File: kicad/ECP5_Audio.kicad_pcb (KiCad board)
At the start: 4 copper layers, 92 x 70 mm, 189 parts, among them J1 HDMI_A, J2 031-71052, J3 USB_B_RECEPTACLE, J4 USB_C_Receptacle, Q1 MMST2222A, SW1 Reset, T1 DA101JC, U1 TPS22948, U10 LP5907MFX-3.3, U11 FT2232HQ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

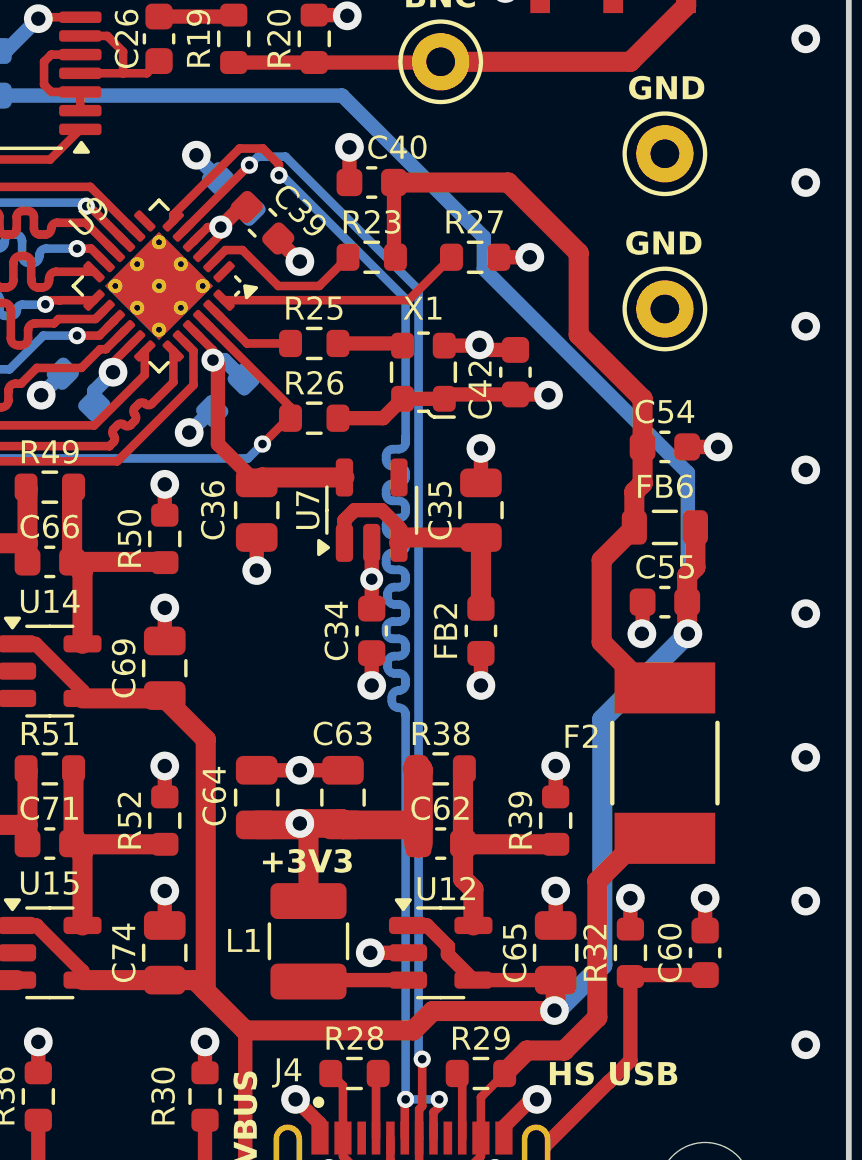
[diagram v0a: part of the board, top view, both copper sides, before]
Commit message: Moved 8.06K resistor close to USB3318C
Moved 8.06K resistor close to USB3318C
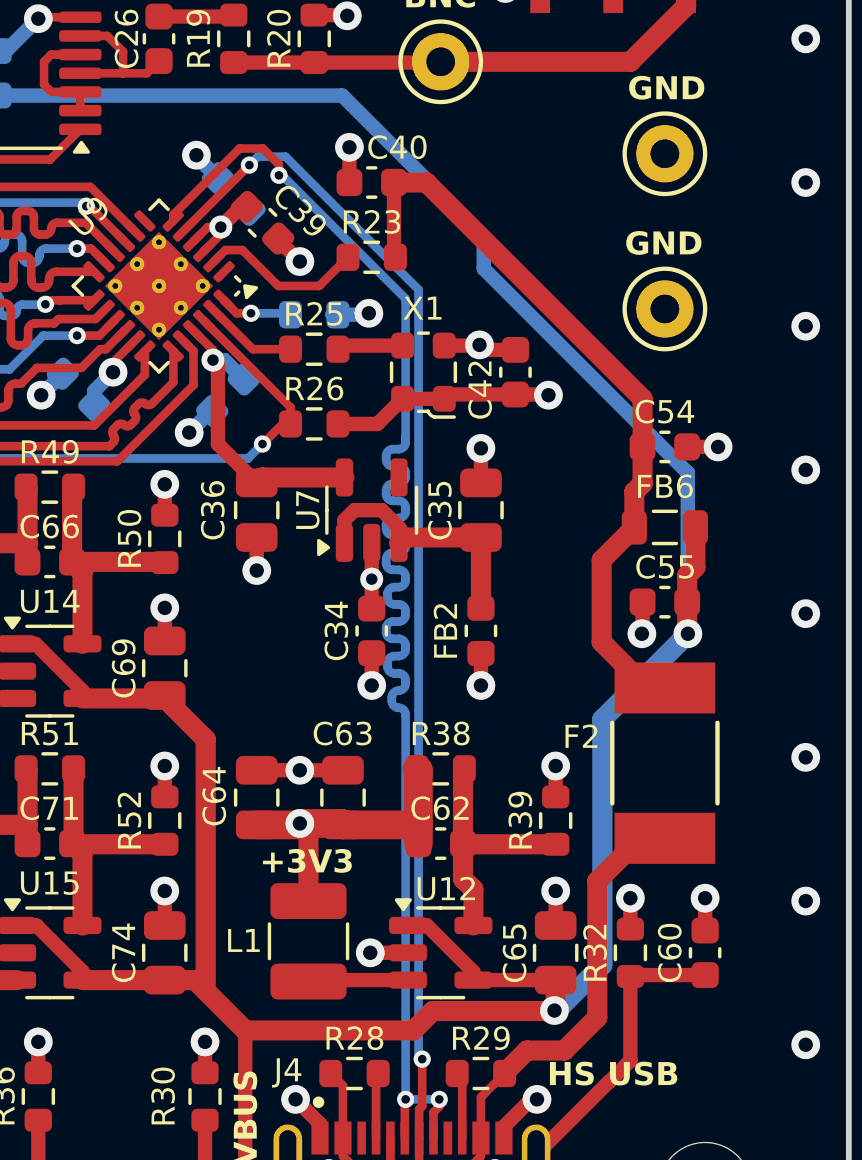
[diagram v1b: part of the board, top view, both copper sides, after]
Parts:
- R27: moved to B.Cu
- moved R27 5.95 mm to (123.4, 84.6)
- moved R25 0.20 mm to (123.4, 85.8)
- moved R26 0.20 mm to (123.4, 88.4)
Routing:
- net Net-(U9-RBIAS): track 8.53 -> 2.53 mm, vias 0 -> 1
- net ULPI_VBUS: track 28.3 -> 26.7 mm

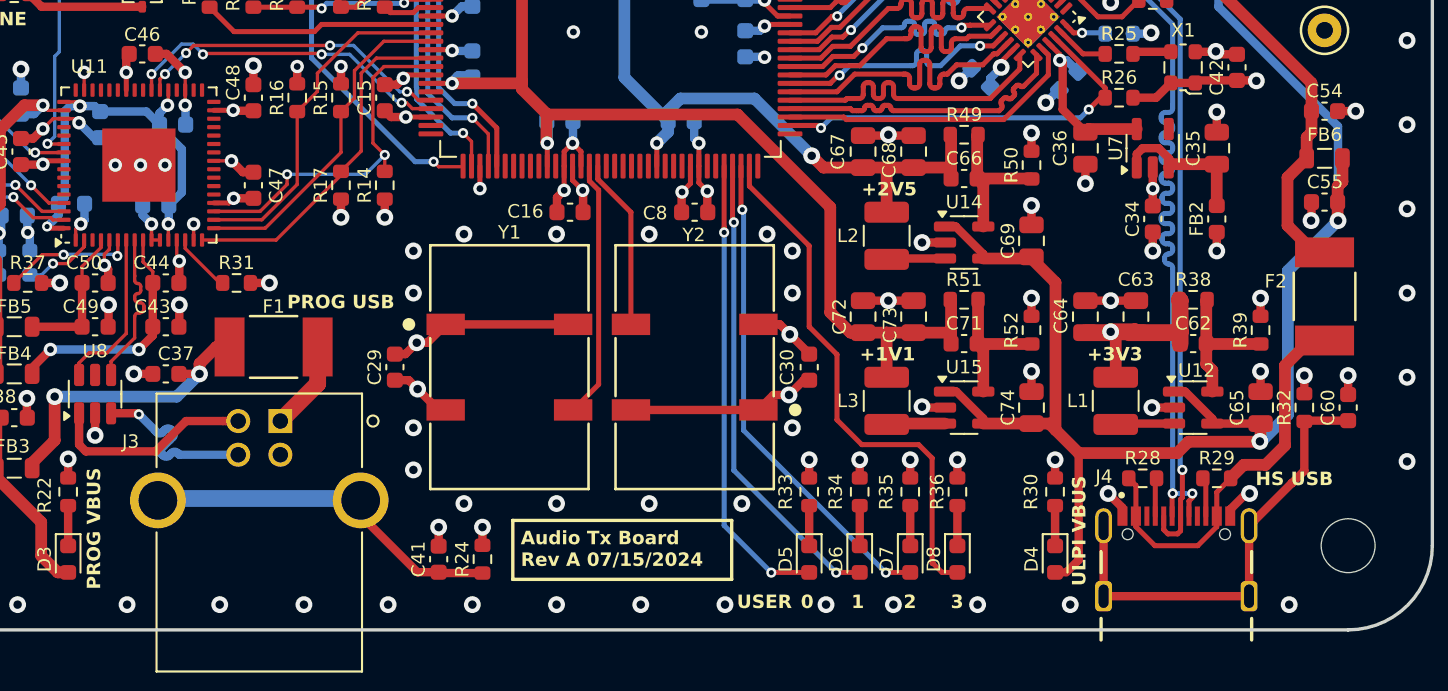
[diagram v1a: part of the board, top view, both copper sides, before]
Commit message: Prepared submission to PCBWay
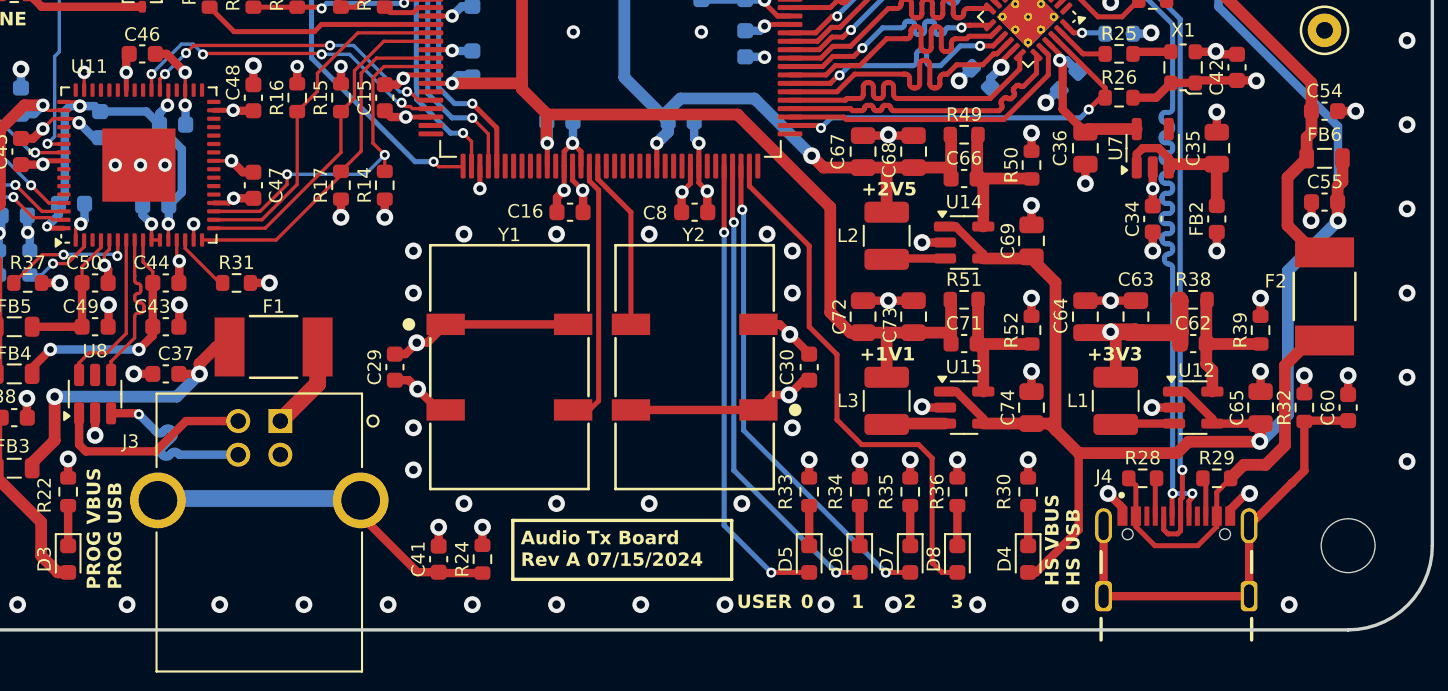
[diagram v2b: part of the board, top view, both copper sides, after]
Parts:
- moved D4 1.60 mm to (118.0, 115.8)
- moved R30 1.60 mm to (118.0, 111.8)
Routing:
- net +5V: track 153.3 -> 154.0 mm
- net 24.576MHz: track 15.3 -> 15.9 mm
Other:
- board text added: "HS VBUS"
- board text removed: "ULPI VBUS"
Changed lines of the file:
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@@
 	(footprint "Resistor_SMD:R_0603_1608Metric"
 		(layer "F.Cu")
-		(at 119.6 111.8 90)
+		(at 118 111.8 90)
 		(descr "Resistor SMD 0603 (1608 Metric), square (rectangular) end terminal, IPC_7351 nominal, (Body size source: IPC-SM-782 page 72, https://www.pcb-3d.com/wordpress/wp-content/uploads/ipc-sm-782a_amendment_1_and_2.pdf), generated with kicad-footprint-generator")
 		(tags "resistor")
@@
 		(tags "CCHD-950-50-100.000 ")
 		(property "Reference" "Y1"
-			(at 0 -8 0)
+			(at 0 -7.85 0)
 			(unlocked yes)
 			(layer "F.SilkS")
@@
 	(footprint "LED_SMD:LED_0603_1608Metric"
 		(layer "F.Cu")
-		(at 119.6 115.8 -90)
+		(at 118 115.8 -90)
 		(descr "LED SMD 0603 (1608 Metric), square (rectangular) end terminal, IPC_7351 nominal, (Body size source: http://www.tortai-tech.com/upload/download/2011102023233369053.pdf), generated with kicad-footprint-generator")
 		(tags "LED")
@@
 		)
 		(property "Value" "8.06K"
-			(at 0 -1.43 360)
+			(at 0 -1.43 0)
 			(layer "B.Fab")
 			(effects
@@
 		)
 		(fp_text user "${REFERENCE}"
-			(at 0 0 360)
+			(at 0 0 0)
 			(layer "B.Fab")
 			(effects
@@
 	)
 	(gr_text "PROG USB"
-		(at 74 101 0)
+		(at 64.25 117.6 90)
 		(layer "F.SilkS" knockout)
 		(effects
@@
 	)
 	(gr_text "HS USB"
-		(at 131.5 111.5 0)
+		(at 121.15 117.4 90)
 		(layer "F.SilkS" knockout)
 		(effects
@@
 		)
 	)
-	(gr_text "ULPI VBUS"
-		(at 121.5 117.4 90)
+	(gr_text "HS VBUS"
+		(at 119.9 117.4 90)
 		(layer "F.SilkS" knockout)
 		(effects
@@
 	)
 	(segment
-		(start 119.6 110.975)
-		(end 119.6 109.9)
+		(start 118 110.975)
+		(end 118 109.9)
 		(width 0.5)
 		(layer "F.Cu")
@@
 	)
 	(via
-		(at 119.6 109.9)
+		(at 118 109.9)
 		(size 1)
 		(drill 0.5)
@@
 	)
 	(segment
-		(start 119.6 116.5875)
-		(end 120.0625 116.5875)
+		(start 118 116.5875)
+		(end 118.4625 116.5875)
 		(width 0.5)
 		(layer "F.Cu")
@@
 	)
 	(segment
+		(start 118.4625 116.5875)
+		(end 121 114.05)
+		(width 0.5)
+		(layer "F.Cu")
+		(net 5)
+	)
+	(segment
 		(start 115.3375 107.75)
 		(end 115.3375 107.450001)
@@
 	)
 	(segment
-		(start 121 115.85)
-		(end 121 109.5)
-		(width 0.5)
-		(layer "F.Cu")
-		(net 5)
-	)
-	(segment
 		(start 136.375 95.675)
 		(end 136.4 95.7)
@@
 	)
 	(segment
+		(start 121 114.05)
+		(end 121 109.5)
+		(width 0.5)
+		(layer "F.Cu")
+		(net 5)
+	)
+	(segment
 		(start 136.375 93.675)
 		(end 136.375 94.6)
@@
 	)
 	(segment
-		(start 120.2625 116.5875)
-		(end 121 115.85)
-		(width 0.5)
-		(layer "F.Cu")
-		(net 5)
-	)
-	(segment
 		(start 126.85 109.5)
 		(end 121 109.5)
@@
 	)
 	(segment
-		(start 119.6 115.0125)
-		(end 119.6 112.625)
+		(start 118 115.0125)
+		(end 118 112.625)
 		(width 0.5)
 		(layer "F.Cu")
@@
 	)
 	(segment
-		(start 69.054 85.773)
-		(end 69 85.827)
+		(start 81.023 88.923)
+		(end 81.309712 88.923)
 		(width 0.2)
 		(layer "F.Cu")
@@
 	)
 	(segment
-		(start 81.086712 88.7)
-		(end 81.436712 89.05)
+		(start 69.054 85.773)
+		(end 69 85.827)
 		(width 0.2)
 		(layer "F.Cu")
@@
 	)
 	(segment
+		(start 81.309712 88.923)
+		(end 81.436712 89.05)
+		(width 0.2)
+		(layer "F.Cu")
+		(net 82)
+	)
+	(segment
 		(start 81.436712 89.05)
 		(end 82.5375 89.05)
@@
 	(segment
 		(start 80.8 88.7)
-		(end 81.086712 88.7)
+		(end 81.023 88.923)
 		(width 0.2)
 		(layer "F.Cu")
@@
 	)
 	(segment
+		(start 92.5 93.892577)
+		(end 92.5 106.4)
+		(width 0.3)
+		(layer "F.Cu")
+		(net 86)
+	)
+	(segment
 		(start 91.95 92.4625)
 		(end 91.95 93.342577)
@@
 	)
 	(segment
-		(start 92.5 93.892577)
-		(end 92.5 105.4246)
+		(start 91.96 106.94)
+		(end 90.9846 106.94)
 		(width 0.3)
 		(layer "F.Cu")
@@
 	)
 	(segment
-		(start 92.5 105.4246)
-		(end 90.9846 106.94)
+		(start 92.5 106.4)
+		(end 91.96 106.94)
 		(width 0.3)
 		(layer "F.Cu")

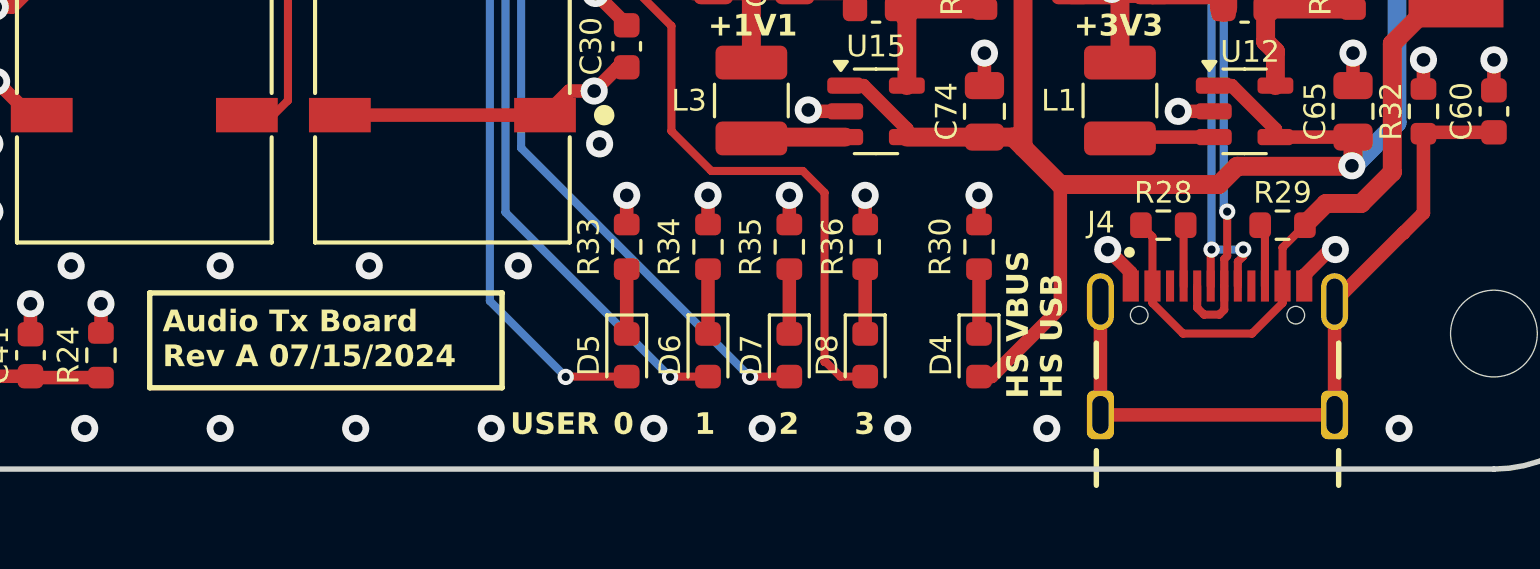
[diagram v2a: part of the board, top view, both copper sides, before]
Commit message: 5.1K USB resistors
Replaces 22K resistors to VBUS with 5.1K resistors to GND.
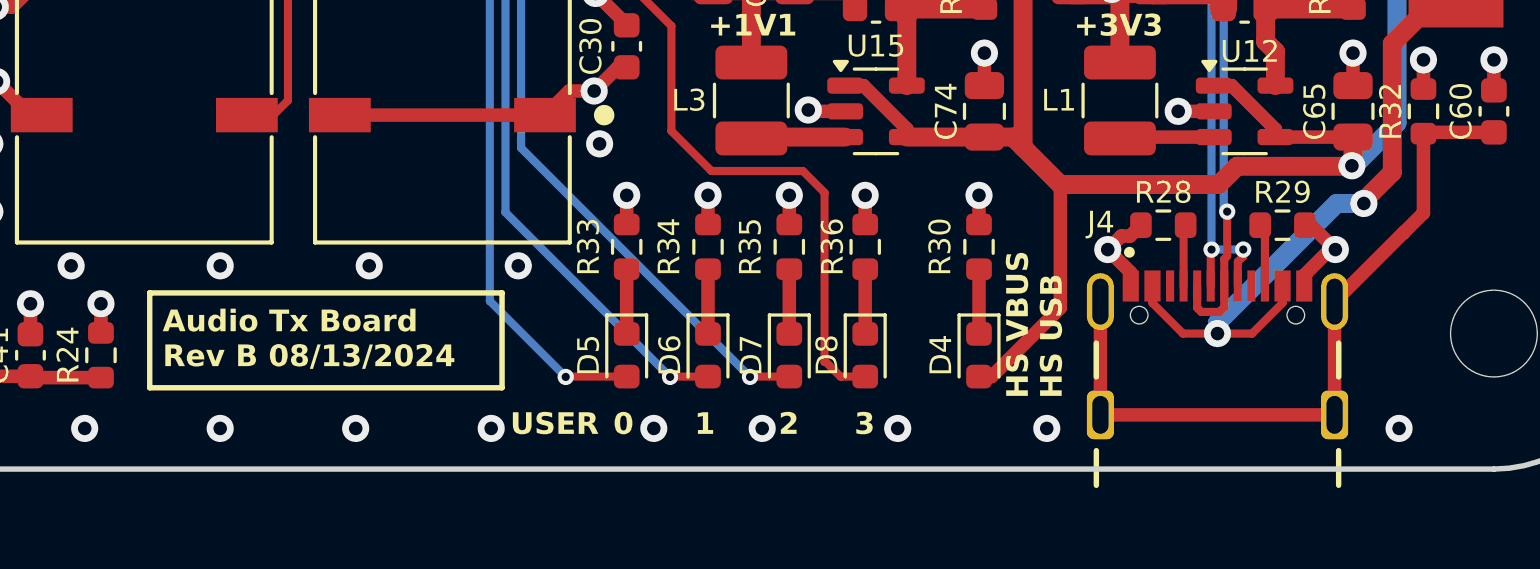
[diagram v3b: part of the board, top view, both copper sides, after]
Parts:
- R28, R29: value 22K -> 5.1K
- U4: value LFE5U-12F-6TG144C -> LFE5U-25F-7TG144C
- turned R28 to 180 degrees
- turned R29 to 0 degrees
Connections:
- R28 pad 1: Net-(F2-Pad2) -> Net-(J4-CC1)
- R28 pad 2: Net-(J4-CC1) -> GND
- R29 pad 1: Net-(F2-Pad2) -> Net-(J4-CC2)
- R29 pad 2: Net-(J4-CC2) -> GND
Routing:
- net GND: track 203.1 -> 206.2 mm
- net Net-(F2-Pad2): track 23.8 -> 24.1 mm, vias 0 -> 2
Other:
- board text added: "Audio Tx Board Rev B 08/13/2024"
- board text removed: "Audio Tx Board Rev A 07/15/2024"
